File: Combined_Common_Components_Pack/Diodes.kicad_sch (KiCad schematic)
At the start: 8 parts

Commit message: More circuits
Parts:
- added D34: SM4007, Diode_SMD:D_MELF, symbol Diode:SM4007
- added D35: D_Bridge, Diode_SMD:Diode_Bridge_Diotec_ABS, symbol Device:D_Bridge_+-AA
- D3: Type SMD -> (none)
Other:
- note added: "Rectifiers"
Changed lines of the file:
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@@
 	(rectangle
 		(start 31.75 29.21)
-		(end 104.14 92.71)
+		(end 104.14 39.37)
 		(stroke
 			(width 0)
@@
 		)
 	)
+	(rectangle
+		(start 58.42 59.69)
+		(end 104.14 85.09)
+		(stroke
+			(width 0)
+			(type default)
+		)
+		(fill
+			(type none)
+		)
+	)
 	(text "For switched regulators"
 		(exclude_from_sim no)
 		(at 73.914 41.91 0)
+		(effects
+			(font
+				(size 1.27 1.27)
+			)
+		)
+	)
+	(text "Rectifiers"
+		(exclude_from_sim no)
+		(at 71.12 62.738 0)
 		(effects
 			(font
@@
 	)
 	(symbol
+		(lib_id "Diode:SM4007")
+		(at 64.77 72.39 270)
+		(unit 1)
+		(exclude_from_sim no)
+		(in_bom yes)
+		(on_board yes)
+		(dnp no)
+		(fields_autoplaced yes)
+		(property "Reference" "D34"
+			(at 67.31 71.1199 90)
+			(effects
+				(font
+					(size 1.27 1.27)
+				)
+				(justify left)
+			)
+		)
+		(property "Value" "SM4007"
+			(at 67.31 73.6599 90)
+			(effects
+				(font
+					(size 1.27 1.27)
+				)
+				(justify left)
+			)
+		)
+		(property "Footprint" "Diode_SMD:D_MELF"
+			(at 60.325 72.39 0)
+			(effects
+				(font
+					(size 1.27 1.27)
+				)
+				(hide yes)
+			)
+		)
+		(property "Datasheet" "http://cdn-reichelt.de/documents/datenblatt/A400/SMD1N400%23DIO.pdf"
+			(at 64.77 72.39 0)
+			(effects
+				(font
+					(size 1.27 1.27)
+				)
+				(hide yes)
+			)
+		)
+		(property "Description" "1000V 1A General Purpose Rectifier Diode, MELF"
+			(at 64.77 72.39 0)
+			(effects
+				(font
+					(size 1.27 1.27)
+				)
+				(hide yes)
+			)
+		)
+		(property "Sim.Device" "D"
+			(at 64.77 72.39 0)
+			(effects
+				(font
+					(size 1.27 1.27)
+				)
+				(hide yes)
+			)
+		)
+		(property "Sim.Pins" "1=K 2=A"
+			(at 64.77 72.39 0)
+			(effects
+				(font
+					(size 1.27 1.27)
+				)
+				(hide yes)
+			)
+		)
+		(pin "2"
+		)
+		(pin "1"
+		)
+		(instances
+			(project "Combined_Common_Components_Pack"
+				(path "/59e42e8e-5444-465a-b7a8-ffbd342a8d49/1381f410-15ba-480c-b8e7-d9f156eccb54"
+					(reference "D34")
+					(unit 1)
+				)
+			)
+		)
+	)
+	(symbol
 		(lib_id "Device:D_Zener")
 		(at 50.8 72.39 270)
@@
 			)
 		)
-		(property "Type" "SMD"
-			(at 52.07 49.53 0)
-			(effects
-				(font
-					(size 1.27 1.27)
-				)
-				(hide yes)
-			)
-		)
 		(property "Manufacturer " "MDD(Microdiode Semiconductor)"
 			(at 52.07 49.53 0)
@@
 			)
 		)
-		(property "Sim.Library" ""
-			(at 99.06 49.53 0)
-			(effects
-				(font
-					(size 1.27 1.27)
-				)
-				(hide yes)
-			)
-		)
-		(property "Sim.Name" ""
-			(at 99.06 49.53 0)
-			(effects
-				(font
-					(size 1.27 1.27)
-				)
-				(hide yes)
-			)
-		)
-		(property "Sim.Params" ""
-			(at 99.06 49.53 0)
-			(effects
-				(font
-					(size 1.27 1.27)
-				)
-				(hide yes)
-			)
-		)
 		(property "Manufacturer " "TWGMC"
 			(at 99.06 49.53 0)
@@
 	)
 	(symbol
+		(lib_id "Device:D_Bridge_+-AA")
+		(at 88.9 73.66 0)
+		(unit 1)
+		(exclude_from_sim no)
+		(in_bom yes)
+		(on_board yes)
+		(dnp no)
+		(property "Reference" "D35"
+			(at 89.154 73.406 0)
+			(effects
+				(font
+					(size 1.27 1.27)
+				)
+			)
+		)
+		(property "Value" "D_Bridge"
+			(at 95.504 68.58 0)
+			(effects
+				(font
+					(size 1.27 1.27)
+				)
+			)
+		)
+		(property "Footprint" "Diode_SMD:Diode_Bridge_Diotec_ABS"
+			(at 88.9 73.66 0)
+			(effects
+				(font
+					(size 1.27 1.27)
+				)
+				(hide yes)
+			)
+		)
+		(property "Datasheet" "https://www.lcsc.com/datasheet/C193012.pdf"
+			(at 88.9 73.66 0)
+			(effects
+				(font
+					(size 1.27 1.27)
+				)
+				(hide yes)
+			)
+		)
+		(property "Description" "Diode bridge, +ve/-ve/AC/AC"
+			(at 88.9 73.66 0)
+			(effects
+				(font
+					(size 1.27 1.27)
+				)
+				(hide yes)
+			)
+		)
+		(property "LCSC" "C193012"
+			(at 88.9 73.66 0)
+			(effects
+				(font
+					(size 1.27 1.27)
+				)
+				(hide yes)
+			)
+		)
+		(pin "4"
+		)
+		(pin "1"
+		)
+		(pin "2"
+		)
+		(pin "3"
+		)
+		(instances
+			(project ""
+				(path "/59e42e8e-5444-465a-b7a8-ffbd342a8d49/1381f410-15ba-480c-b8e7-d9f156eccb54"
+					(reference "D35")
+					(unit 1)
+				)
+			)
+		)
+	)
+	(symbol
 		(lib_id "Diode:BAT54S")
 		(at 39.37 73.66 270)
@@
 			(at 38.1 49.53 0)
 			(effects
-				(font
-					(size 1.27 1.27)
-				)
-				(hide yes)
-			)
-		)
-		(property "TYPE" ""
-			(at 38.1 49.53 0)
-			(effects

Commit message: Added some connectors and basic parts
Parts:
- added D40: 1N4148W, Diode_SMD:D_SOD-123, symbol Diode:1N4148W
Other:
- note added: "Basic"
- note added: "Extended"
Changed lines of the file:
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@@
 	(paper "A4")
 	(rectangle
-		(start 31.75 39.37)
+		(start 21.59 39.37)
 		(end 58.42 59.69)
 		(stroke
@@
 	)
 	(rectangle
-		(start 31.75 59.69)
+		(start 21.59 59.69)
 		(end 58.42 85.09)
 		(stroke
@@
 		)
 	)
+	(text "Extended"
+		(exclude_from_sim no)
+		(at 46.228 50.546 90)
+		(effects
+			(font
+				(size 1.27 1.27)
+			)
+		)
+	)
+	(text "Basic"
+		(exclude_from_sim no)
+		(at 28.194 55.88 0)
+		(effects
+			(font
+				(size 1.27 1.27)
+			)
+		)
+	)
 	(text "For signal and flywheel"
 		(exclude_from_sim no)
-		(at 45.466 41.656 0)
+		(at 38.862 42.164 0)
 		(effects
 			(font
@@
 					(unit 1)
 				)
+			)
+		)
+	)
+	(symbol
+		(lib_id "Diode:1N4148W")
+		(at 27.94 49.53 270)
+		(unit 1)
+		(exclude_from_sim no)
+		(in_bom yes)
+		(on_board yes)
+		(dnp no)
+		(property "Reference" "D40"
+			(at 23.622 46.99 90)
+			(effects
+				(font
+					(size 1.27 1.27)
+				)
+				(justify left)
+			)
+		)
+		(property "Value" "1N4148W"
+			(at 30.988 54.356 0)
+			(effects
+				(font
+					(size 1.27 1.27)
+				)
+				(justify right)
+			)
+		)
+		(property "Footprint" "Diode_SMD:D_SOD-123"
+			(at 23.495 49.53 0)
+			(effects
+				(font
+					(size 1.27 1.27)
+				)
+				(hide yes)
+			)
+		)
+		(property "Datasheet" "https://www.vishay.com/docs/85748/1n4148w.pdf"
+			(at 27.94 49.53 0)
+			(effects
+				(font
+					(size 1.27 1.27)
+				)
+				(hide yes)
+			)
+		)
+		(property "Description" "Diode Independent 100V 300mA Surface Mount SOD-123"
+			(at 27.94 49.53 0)
+			(effects
+				(font
+					(size 1.27 1.27)
+				)
+				(hide yes)
+			)
+		)
+		(property "LCSC" "C81598"
+			(at 27.94 49.53 0)
+			(effects
+				(font
+					(size 1.27 1.27)
+				)
+				(hide yes)
+			)
+		)
+		(property "Manufacturer " " ST(Semtech)"
+			(at 27.94 49.53 0)
+			(effects
+				(font
+					(size 1.27 1.27)
+				)
+				(hide yes)
+			)
+		)
+		(property "Mfr. Part Number" "1N4148W"
+			(at 27.94 49.53 0)
+			(effects
+				(font
+					(size 1.27 1.27)
+				)
+				(hide yes)
+			)
+		)
+		(property "Observations" "1V@150mA"
+			(at 33.02 50.546 0)
+			(effects
+				(font
+					(size 1.27 1.27)
+				)
+			)
+		)
+		(pin "2"
+		)
+		(pin "1"
+		)
+		(instances
+			(project "Combined_Common_Components_Pack"
+				(path "/59e42e8e-5444-465a-b7a8-ffbd342a8d49/1381f410-15ba-480c-b8e7-d9f156eccb54"
+					(reference "D40")
+					(unit 1)
+				)

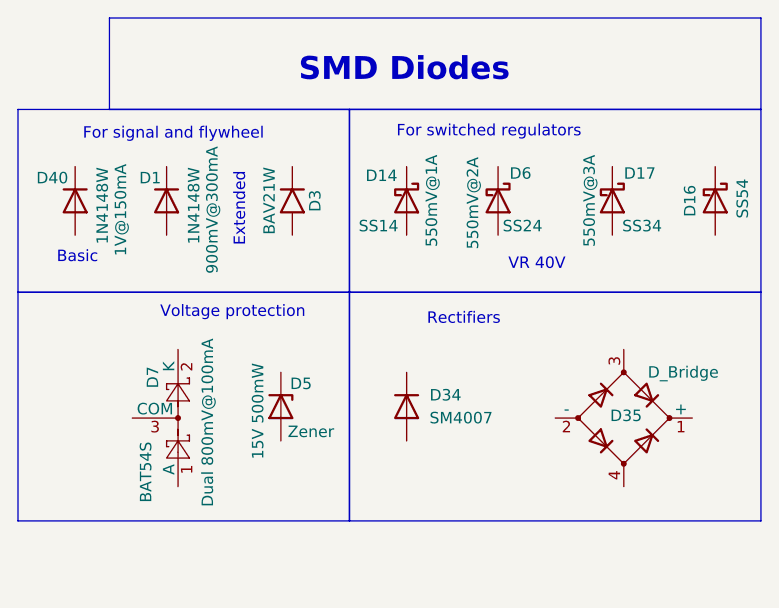
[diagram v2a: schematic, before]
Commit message: Minor updates
Basically components annotation, and more basic parts added
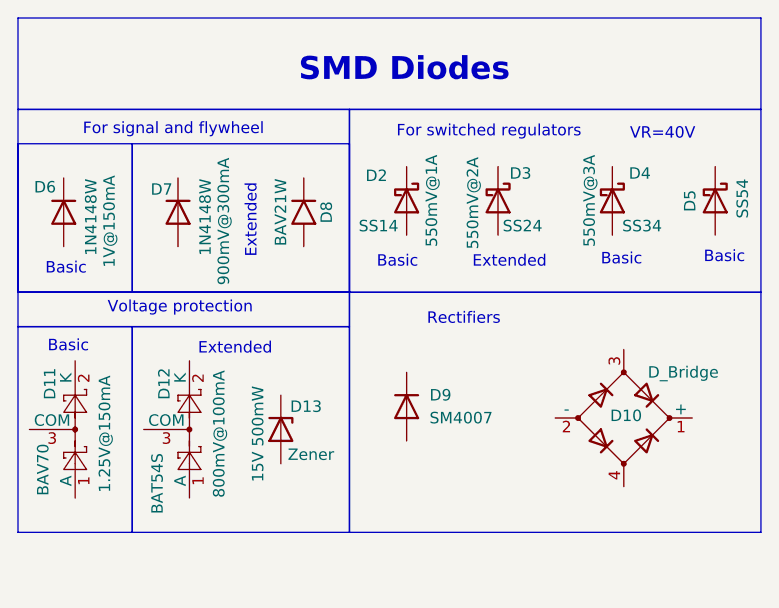
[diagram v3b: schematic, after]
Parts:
- added D11: BAV70, Package_TO_SOT_SMD:SOT-23, symbol Diode:BAT54S
- D12: renamed from D7; Observations Dual 800mV@100mA -> 800mV@100mA
- D2: renamed from D14; LCSC C2909920 -> C2480
- D5: renamed from D16; LCSC C727065 -> C22452
- D9: renamed from D34; LCSC (none) -> C64898
- renumbered D35 to D10, D5 to D13, D6 to D3, D17 to D4, D40 to D6, D1 to D7, D3 to D8
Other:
- note added: "VR=40V"
- note removed: "VR 40V"
- moved on the sheet: D12, D13, D6, D7, D8
